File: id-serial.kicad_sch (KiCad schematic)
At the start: 5 parts, among them IC17 AT24CS01-ST

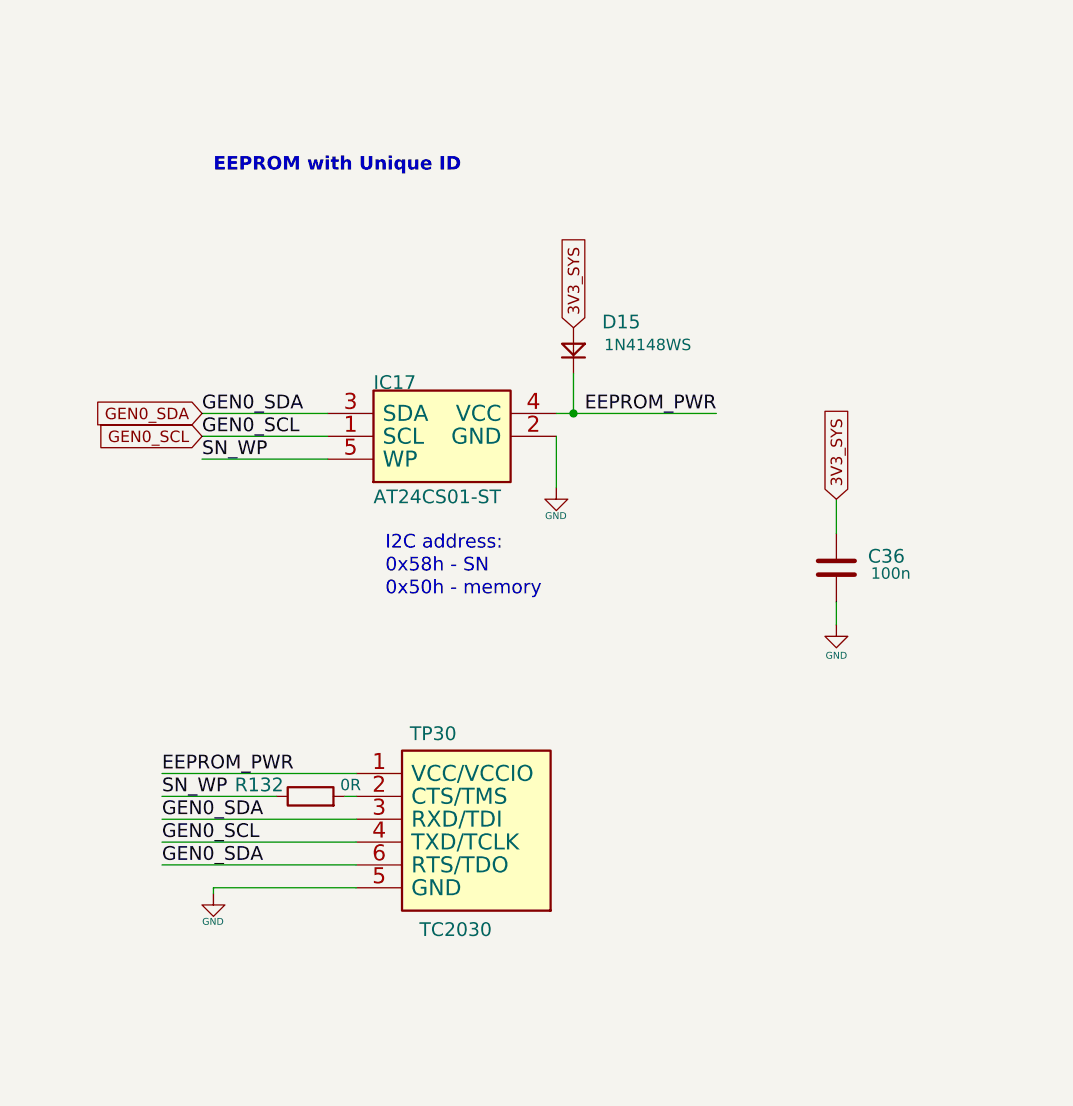
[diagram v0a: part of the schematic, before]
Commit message: Standardize components
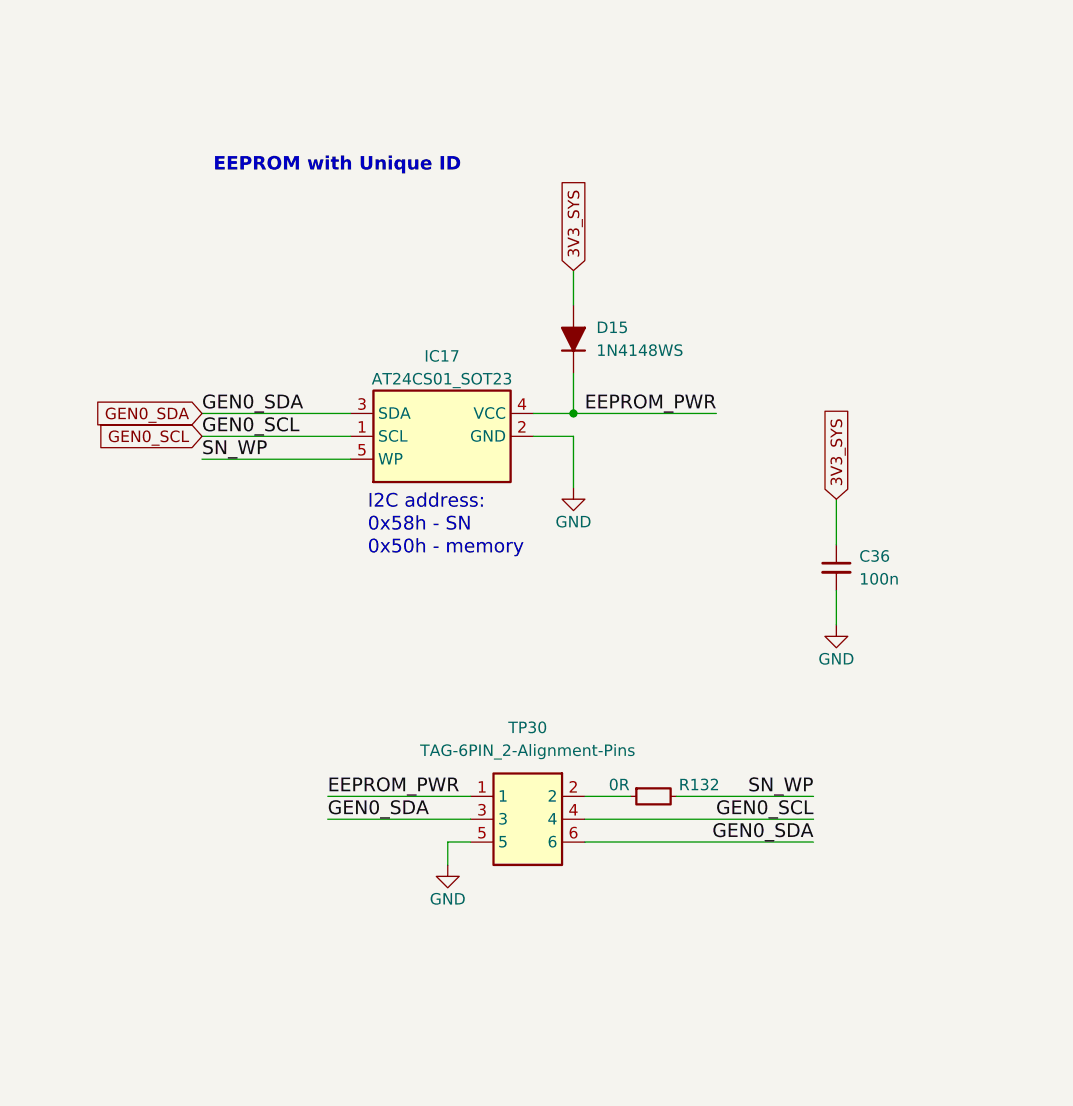
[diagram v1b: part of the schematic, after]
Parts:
- removed IC17: AT24CS01-ST, jetson-nano-baseboard-footprints:SOT23-5, symbol jetson-nano-baseboard:AT24CS01
- added IC17: AT24CS01_SOT23, antmicro-footprints:SOT-23-5, symbol antmicroMemory:AT24CS01_SOT23
- C36: footprint jetson-nano-baseboard-footprints:0402-cap -> antmicro-footprints:C_0402_1005Metric; symbol jetson-nano-baseboard:C_100n_0402 -> antmicroCapacitors0402:C_100n_0402; Author (none) -> Antmicro; Dielectric (none) -> X5R; License (none) -> Apache-2.0; MPN 0402X104K6R3CT -> GRM155R61H104KE14D; Manufacturer Walsin -> Murata; Voltage (none) -> 50V
- D15: value diode -> 1N4148WS; footprint jetson-nano-baseboard-footprints:SOD-323 -> antmicro-footprints:D_SOD-323F; symbol jetson-nano-baseboard:diode -> antmicroDiodesRectifiersSingle:1N4148WS; Author (none) -> Antmicro; License (none) -> Apache-2.0
- R132: footprint jetson-nano-baseboard-footprints:0402-res -> antmicro-footprints:R_0402_1005Metric; symbol jetson-nano-baseboard:R_0R_0402 -> antmicroResistors0402:R_0R_0402; Author (none) -> Antmicro; Current (none) -> 1A; License (none) -> Apache-2.0; Manufacturer PANASONIC -> Panasonic
- TP30: value TC2030 -> TAG-6PIN_2-Alignment-Pins; footprint jetson-nano-baseboard-footprints:TC2030 -> antmicro-footprints:Tag-Connect_TC2030-IDC-NL_2x03_P1.27mm_2-alignment-holes; symbol jetson-nano-baseboard:TC2030 -> antmicroTestPoints:TAG-6PIN_2-Alignment-Pins; Author (none) -> Antmicro; License (none) -> Apache-2.0; MPN TC2030 -> (none); Manufacturer Tag Connect -> (none)
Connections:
- net 3V3_SYS: now also C36.1; no longer C36.2
- net EEPROM_PWR: now also D15.K, IC17.4 (VCC); no longer D15.C
- net GEN0_SCL: now also IC17.1 (SCL)
- net GEN0_SDA: now also IC17.3 (SDA)
- net GND: now also C36.2, IC17.2 (GND); no longer C36.1
- net SN_WP: now also R132.2, IC17.5 (WP); no longer R132.1
- net at TP30.2: now also R132.1; no longer R132.2
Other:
- moved on the sheet: C36, R132, TP30

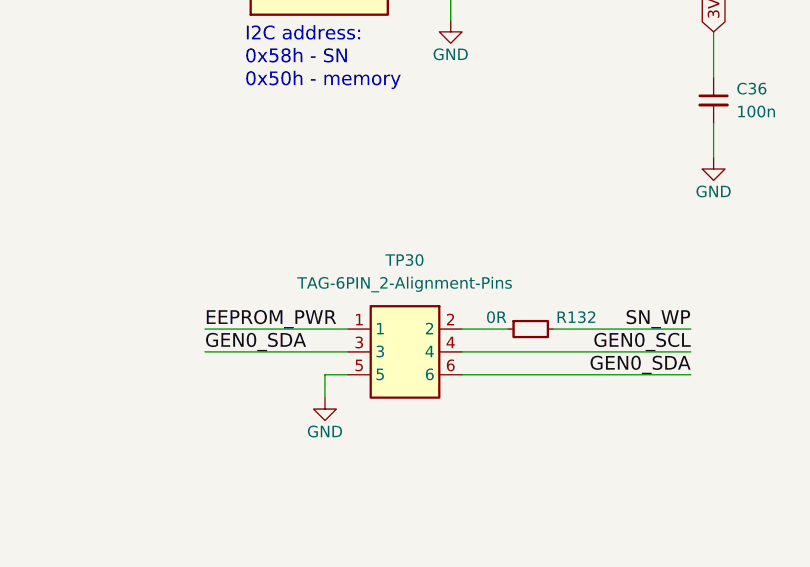
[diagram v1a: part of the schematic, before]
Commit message: [#56834] Fix components links
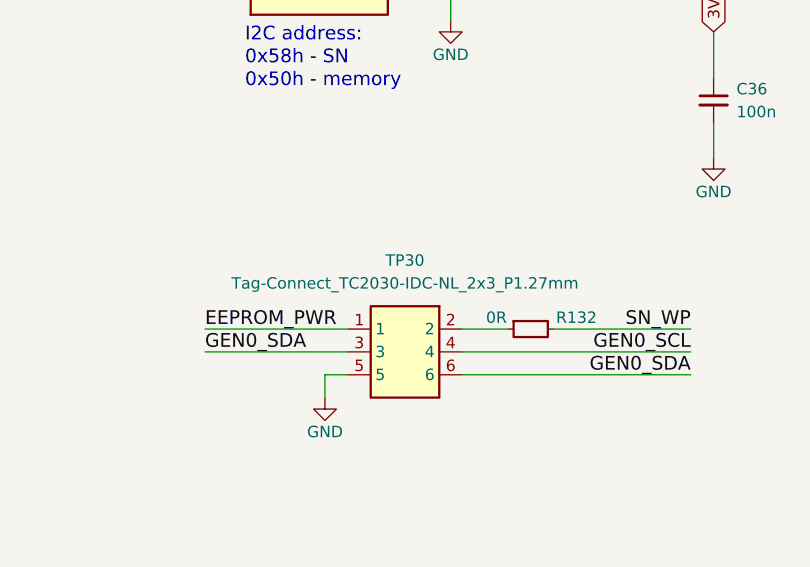
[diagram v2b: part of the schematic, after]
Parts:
- C36: footprint antmicro-footprints:C_0402_1005Metric -> jetson-nano-baseboard-footprints:C_0402_1005Metric; symbol antmicroCapacitors0402:C_100n_0402 -> jetson-nano-baseboard:C_100n_0402
- D15: footprint antmicro-footprints:D_SOD-323F -> jetson-nano-baseboard-footprints:D_SOD-323F; symbol antmicroDiodesRectifiersSingle:1N4148WS -> jetson-nano-baseboard:1N4148WS
- IC17: footprint antmicro-footprints:SOT-23-5 -> jetson-nano-baseboard-footprints:SOT-23-5; symbol antmicroMemory:AT24CS01_SOT23 -> jetson-nano-baseboard:AT24CS01_SOT23
- R132: footprint antmicro-footprints:R_0402_1005Metric -> jetson-nano-baseboard-footprints:R_0402_1005Metric; symbol antmicroResistors0402:R_0R_0402 -> jetson-nano-baseboard:R_0R_0402
- TP30: value TAG-6PIN_2-Alignment-Pins -> Tag-Connect_TC2030-IDC-NL_2x3_P1.27mm; footprint antmicro-footprints:Tag-Connect_TC2030-IDC-NL_2x03_P1.27mm_2-alignment-holes -> jetson-nano-baseboard-footprints:Tag-Connect_TC2030-IDC-NL_2x3_P1.27mm; symbol antmicroTestPoints:TAG-6PIN_2-Alignment-Pins -> jetson-nano-baseboard:Tag-Connect_TC2030-IDC-NL_2x3_P1.27mm; MPN (none) -> TC2030-IDC-NL; Manufacturer (none) -> Tag Connect

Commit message: [#57913] fix 2309413-1
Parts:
- C36: footprint jetson-nano-baseboard-footprints:C_0402_1005Metric -> antmicro-footprints:C_0402_1005Metric; symbol jetson-nano-baseboard:C_100n_0402 -> antmicroCapacitors0402:C_100n_0402
- D15: footprint jetson-nano-baseboard-footprints:D_SOD-323F -> antmicro-footprints:D_SOD-323F; symbol jetson-nano-baseboard:1N4148WS -> antmicroDiodesRectifiersSingle:1N4148WS
- IC17: footprint jetson-nano-baseboard-footprints:SOT-23-5 -> antmicro-footprints:SOT-23-5; symbol jetson-nano-baseboard:AT24CS01_SOT23 -> antmicroMemory:AT24CS01_SOT23
- R132: footprint jetson-nano-baseboard-footprints:R_0402_1005Metric -> antmicro-footprints:R_0402_1005Metric; symbol jetson-nano-baseboard:R_0R_0402 -> antmicroResistors0402:R_0R_0402
- TP30: footprint jetson-nano-baseboard-footprints:Tag-Connect_TC2030-IDC-NL_2x3_P1.27mm -> antmicro-footprints:Tag-Connect_TC2030-IDC-NL_2x3_P1.27mm; symbol jetson-nano-baseboard:Tag-Connect_TC2030-IDC-NL_2x3_P1.27mm -> antmicroTestPoints:Tag-Connect_TC2030-IDC-NL_2x3_P1.27mm
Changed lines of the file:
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@@
     )
   )
-  (symbol (lib_id "jetson-nano-baseboard:GND") (at 218.44 128.27 0) (unit 1)
+  (symbol (lib_id "antmicropower:GND") (at 218.44 128.27 0) (unit 1)
     (in_bom yes) (on_board yes) (dnp no)
     (property "Reference" "#GND_035" (at 218.44 128.27 0)
@@
     )
   )
-  (symbol (lib_id "jetson-nano-baseboard:GND") (at 247.65 143.51 0) (unit 1)
+  (symbol (lib_id "antmicropower:GND") (at 247.65 143.51 0) (unit 1)
     (in_bom yes) (on_board yes) (dnp no)
     (property "Reference" "#GND_0155" (at 247.65 143.51 0)
@@
     )
   )
-  (symbol (lib_id "jetson-nano-baseboard:1N4148WS") (at 218.44 107.95 270) (unit 1)
+  (symbol (lib_id "antmicroDiodesRectifiersSingle:1N4148WS") (at 218.44 107.95 270) (unit 1)
     (in_bom yes) (on_board yes) (dnp no) (fields_autoplaced)
     (property "Reference" "D15" (at 220.98 110.4899 90)
@@
       (effects (font (size 1.27 1.27)) (justify left) hide)
     )
-    (property "Footprint" "jetson-nano-baseboard-footprints:D_SOD-323F" (at 218.44 107.95 0)
+    (property "Footprint" "antmicro-footprints:D_SOD-323F" (at 218.44 107.95 0)
       (effects (font (size 1.27 1.27)) (justify left) hide)
     )
@@
     )
   )
-  (symbol (lib_id "jetson-nano-baseboard:Tag-Connect_TC2030-IDC-NL_2x3_P1.27mm") (at 207.01 162.56 0) (unit 1)
+  (symbol (lib_id "antmicroTestPoints:Tag-Connect_TC2030-IDC-NL_2x3_P1.27mm") (at 207.01 162.56 0) (unit 1)
     (in_bom yes) (on_board yes) (dnp no) (fields_autoplaced)
     (property "Reference" "TP30" (at 213.36 154.94 0)
@@
       (effects (font (size 1.27 1.27) (thickness 0.15)))
     )
-    (property "Footprint" "jetson-nano-baseboard-footprints:Tag-Connect_TC2030-IDC-NL_2x3_P1.27mm" (at 233.68 170.18 0)
+    (property "Footprint" "antmicro-footprints:Tag-Connect_TC2030-IDC-NL_2x3_P1.27mm" (at 233.68 170.18 0)
       (effects (font (size 1.27 1.27) (thickness 0.15)) (justify left bottom) hide)
     )
@@
     )
   )
-  (symbol (lib_id "jetson-nano-baseboard:GND") (at 204.47 170.18 0) (unit 1)
+  (symbol (lib_id "antmicropower:GND") (at 204.47 170.18 0) (unit 1)
     (in_bom yes) (on_board yes) (dnp no)
     (property "Reference" "#GND_0119" (at 204.47 170.18 0)
@@
     )
   )
-  (symbol (lib_id "jetson-nano-baseboard:R_0R_0402") (at 224.79 162.56 0) (unit 1)
+  (symbol (lib_id "antmicroResistors0402:R_0R_0402") (at 224.79 162.56 0) (unit 1)
     (in_bom yes) (on_board yes) (dnp no)
     (property "Reference" "R132" (at 232.41 161.29 0)
@@
       (effects (font (size 1.27 1.27)) (justify left) hide)
     )
-    (property "Footprint" "jetson-nano-baseboard-footprints:R_0402_1005Metric" (at 229.87 157.48 0)
+    (property "Footprint" "antmicro-footprints:R_0402_1005Metric" (at 229.87 157.48 0)
       (effects (font (size 1.27 1.27)) (justify left) hide)
     )
@@
     )
   )
-  (symbol (lib_id "jetson-nano-baseboard:C_100n_0402") (at 247.65 134.62 270) (unit 1)
+  (symbol (lib_id "antmicroCapacitors0402:C_100n_0402") (at 247.65 134.62 270) (unit 1)
     (in_bom yes) (on_board yes) (dnp no) (fields_autoplaced)
     (property "Reference" "C36" (at 250.19 135.8962 90)
@@
       (effects (font (size 1.27 1.27)) (justify left) hide)
     )
-    (property "Footprint" "jetson-nano-baseboard-footprints:C_0402_1005Metric" (at 252.73 139.7 0)
+    (property "Footprint" "antmicro-footprints:C_0402_1005Metric" (at 252.73 139.7 0)
       (effects (font (size 1.27 1.27)) (justify left) hide)
     )
@@
     )
   )
-  (symbol (lib_id "jetson-nano-baseboard:AT24CS01_SOT23") (at 193.675 120.015 0) (unit 1)
+  (symbol (lib_id "antmicroMemory:AT24CS01_SOT23") (at 193.675 120.015 0) (unit 1)
     (in_bom yes) (on_board yes) (dnp no)
     (property "Reference" "IC17" (at 203.835 113.665 0)
@@
       (effects (font (size 1.27 1.27) (thickness 0.15)))
     )
-    (property "Footprint" "jetson-nano-baseboard-footprints:SOT-23-5" (at 229.235 127.635 0)
+    (property "Footprint" "antmicro-footprints:SOT-23-5" (at 229.235 127.635 0)
       (effects (font (size 1.27 1.27) (thickness 0.15)) (justify left) hide)
     )
